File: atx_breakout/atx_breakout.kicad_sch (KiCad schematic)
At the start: 1 part, among them J1 ATX-24

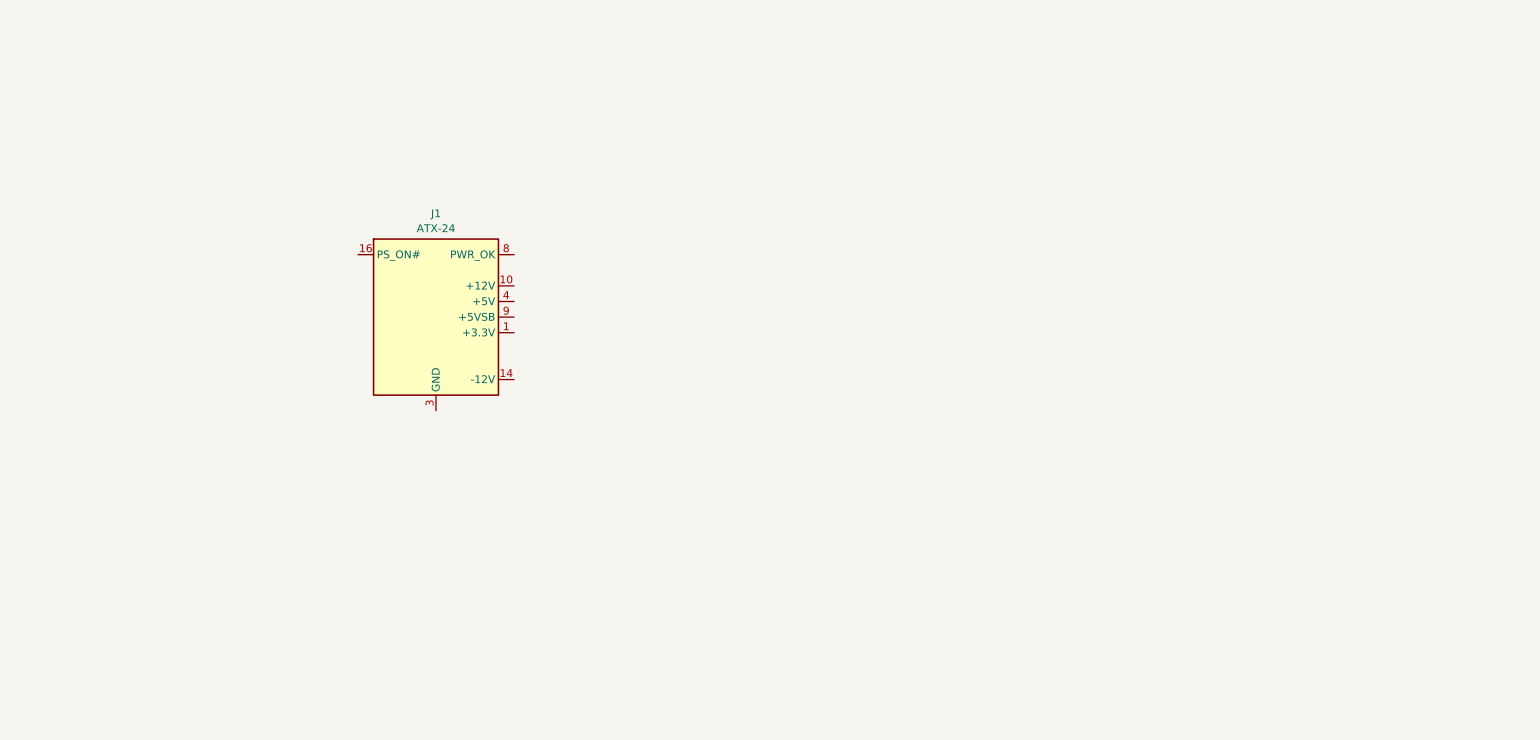
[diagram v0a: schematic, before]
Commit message: Progress on atx breakout
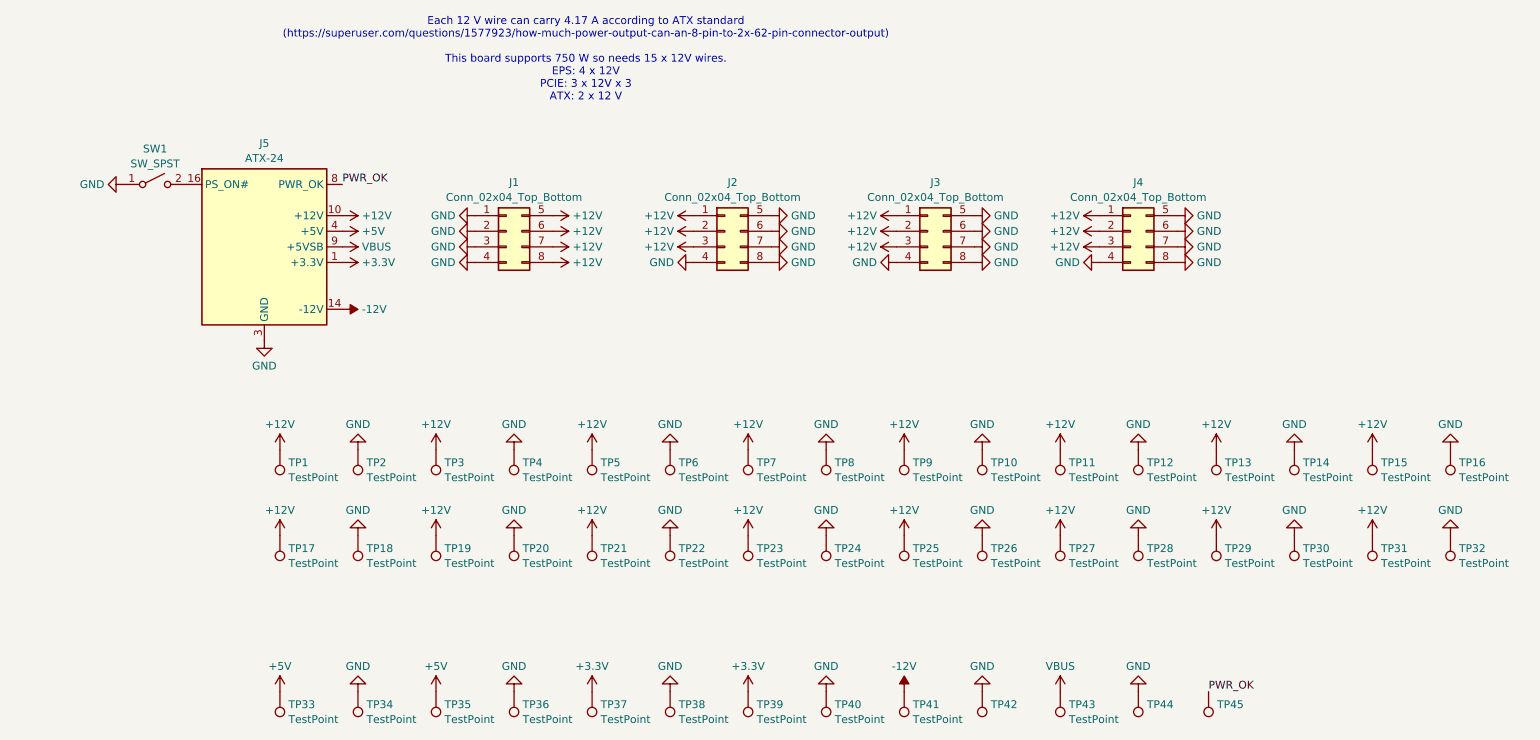
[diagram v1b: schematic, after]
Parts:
- added J1, J2, J3, J4: Conn_02x04_Top_Bottom, Connector_Molex:Molex_Mini-Fit_Jr_5566-08A_2x04_P4.20mm_Vertical, symbol Connector_Generic:Conn_02x04_Top_Bottom
- added SW1: SW_SPST, Button_Switch_THT:SW_PUSH_6mm, symbol Switch:SW_SPST
- added TP1, TP10, TP11, TP12, TP13, TP14, TP15, TP16, TP2, TP3, TP33, TP34, TP35, TP36, TP37, TP38, TP39, TP4, TP40, TP41, TP42, TP43, TP44, TP45, TP5, TP6, TP7, TP8, TP9: TestPoint, TestPoint:TestPoint_THTPad_D1.5mm_Drill0.7mm, symbol Connector:TestPoint
- added TP17, TP18, TP19, TP20, TP21, TP22, TP23, TP24, TP25, TP26, TP27, TP28, TP29, TP30, TP31, TP32: TestPoint, TestPoint:TestPoint_THTPad_D3.0mm_Drill1.5mm, symbol Connector:TestPoint
- renumbered J1 to J5
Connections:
- net +3.3V: now reaches J5.1 (+3.3V), J5.12 (+3.3V), J5.13 (+3.3V), J5.2 (+3.3V)
- net +3.3V: now also TP37.1, TP39.1
- net +12V: now reaches J5.10 (+12V), J5.11 (+12V)
- net +12V: now also J1.5 (Pin_5), J1.6 (Pin_6), J1.7 (Pin_7), J1.8 (Pin_8), J2.1 (Pin_1), J2.2 (Pin_2), J2.3 (Pin_3), J3.1 (Pin_1), J3.2 (Pin_2), J3.3 (Pin_3), J4.1 (Pin_1), J4.2 (Pin_2), J4.3 (Pin_3), TP1.1, TP11.1, TP13.1, TP15.1, TP17.1, TP19.1, TP21.1, TP23.1, TP25.1, TP27.1, TP29.1, TP3.1, TP31.1, TP5.1, TP7.1, TP9.1
- net -12V: now reaches J5.14 (-12V)
- net -12V: now also TP41.1
- net GND: now reaches J5.15 (GND), J5.17 (GND), J5.18 (GND), J5.19 (GND), J5.24 (GND), J5.3 (GND), J5.5 (GND), J5.7 (GND)
- net GND: now also J1.1 (Pin_1), J1.2 (Pin_2), J1.3 (Pin_3), J1.4 (Pin_4), J2.4 (Pin_4), J2.5 (Pin_5), J2.6 (Pin_6), J2.7 (Pin_7), J2.8 (Pin_8), J3.4 (Pin_4), J3.5 (Pin_5), J3.6 (Pin_6), J3.7 (Pin_7), J3.8 (Pin_8), J4.4 (Pin_4), J4.5 (Pin_5), J4.6 (Pin_6), J4.7 (Pin_7), J4.8 (Pin_8), SW1.1 (A), TP10.1, TP12.1, TP14.1, TP16.1, TP18.1, TP2.1, TP20.1, TP22.1, TP24.1, TP26.1, TP28.1, TP30.1, TP32.1, TP34.1, TP36.1, TP38.1, TP4.1, TP40.1, TP42.1, TP44.1, TP6.1, TP8.1
- net at J5.16 (PS_ON#): now also SW1.2 (B)
- net +5V: now reaches J5.21 (+5V), J5.22 (+5V), J5.23 (+5V), J5.4 (+5V), J5.6 (+5V)
- net +5V: now also TP33.1, TP35.1
- net PWR_OK: now reaches J5.8 (PWR_OK)
- net PWR_OK: now also TP45.1
- net VBUS: now reaches J5.9 (+5VSB)
- net VBUS: now also TP43.1
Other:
- note added: "Each 12 V wire can carry 4.17 A according to ATX standard (https://superuser.com/questions/1577923/how-much-power-output-can-an-8-pin-to-2x-62-pin-connector-output) This board supports 750 W so needs 15 x 12V wires. EPS: 4 x 12V PCIE: 3 x 12V x 3 ATX: 2 x 12 V"
- moved on the sheet: J5

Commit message: Progress on atx breakout
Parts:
- added H1: MountingHole, MountingHole:MountingHole_2.2mm_M2, symbol Mechanical:MountingHole
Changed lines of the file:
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@@
+	)
+	(symbol
+		(lib_id "Mechanical:MountingHole")
+		(at 190.5 49.53 0)
+		(unit 1)
+		(exclude_from_sim yes)
+		(in_bom no)
+		(on_board yes)
+		(dnp no)
+		(fields_autoplaced yes)
+		(property "Reference" "H1"
+			(at 193.04 48.3178 0)
+			(effects
+				(font
+					(size 1.27 1.27)
+				)
+				(justify left)
+			)
+		)
+		(property "Value" "MountingHole"
+			(at 193.04 50.7421 0)
+			(effects
+				(font
+					(size 1.27 1.27)
+				)
+				(justify left)
+			)
+		)
+		(property "Footprint" "MountingHole:MountingHole_2.2mm_M2"
+			(at 190.5 49.53 0)
+			(effects
+				(font
+					(size 1.27 1.27)
+				)
+				(hide yes)
+			)
+		)
+		(property "Datasheet" "~"
+			(at 190.5 49.53 0)
+			(effects
+				(font
+					(size 1.27 1.27)
+				)
+				(hide yes)
+			)
+		)
+		(property "Description" "Mounting Hole without connection"
+			(at 190.5 49.53 0)
+			(effects
+				(font
+					(size 1.27 1.27)
+				)
+				(hide yes)
+			)
+		)
+		(instances
+			(project ""
+				(path "/8bcbfe75-aa60-4e26-b080-e95e33d1efa7"
+					(reference "H1")
+					(unit 1)
+				)
+			)
+		)
 	)
 	(symbol

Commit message: Finished atx breakout
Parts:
- removed SW1: SW_SPST, Button_Switch_THT:SW_PUSH_6mm, symbol Switch:SW_SPST
- added U1: SW_DPDT_PS-70N, misc:SW_DPDT_PS-70N, symbol misc:SW_DPDT_PS-70N
- J1, J2, J3, J4: footprint Connector_Molex:Molex_Mini-Fit_Jr_5566-08A_2x04_P4.20mm_Vertical -> misc:Molex_Mini-Fit_Jr_5566-08A_2x04_P4.20mm_XY_Vertical
- J5: footprint Connector_Molex:Molex_Mini-Fit_Jr_5566-24A_2x12_P4.20mm_Vertical -> misc:Molex_Mini-Fit_Jr_5566-24A_2x12_P4.20mm_XY_Vertical
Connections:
- net GND: now also U1.1, U1.2, U1.4, U1.5, U1.6
- net at J5.16 (PS_ON#): now also U1.3

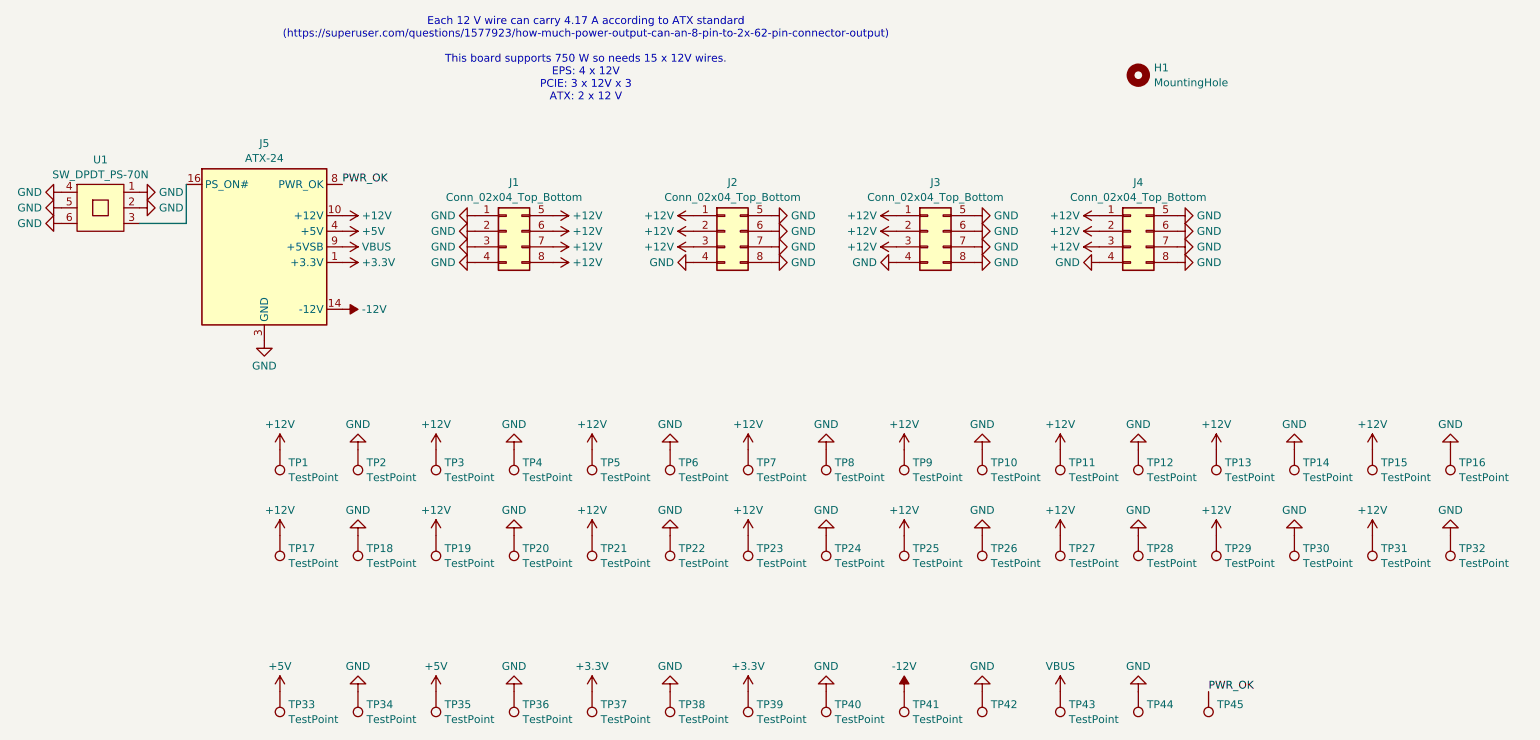
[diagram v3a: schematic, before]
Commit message: Add atx gerbers
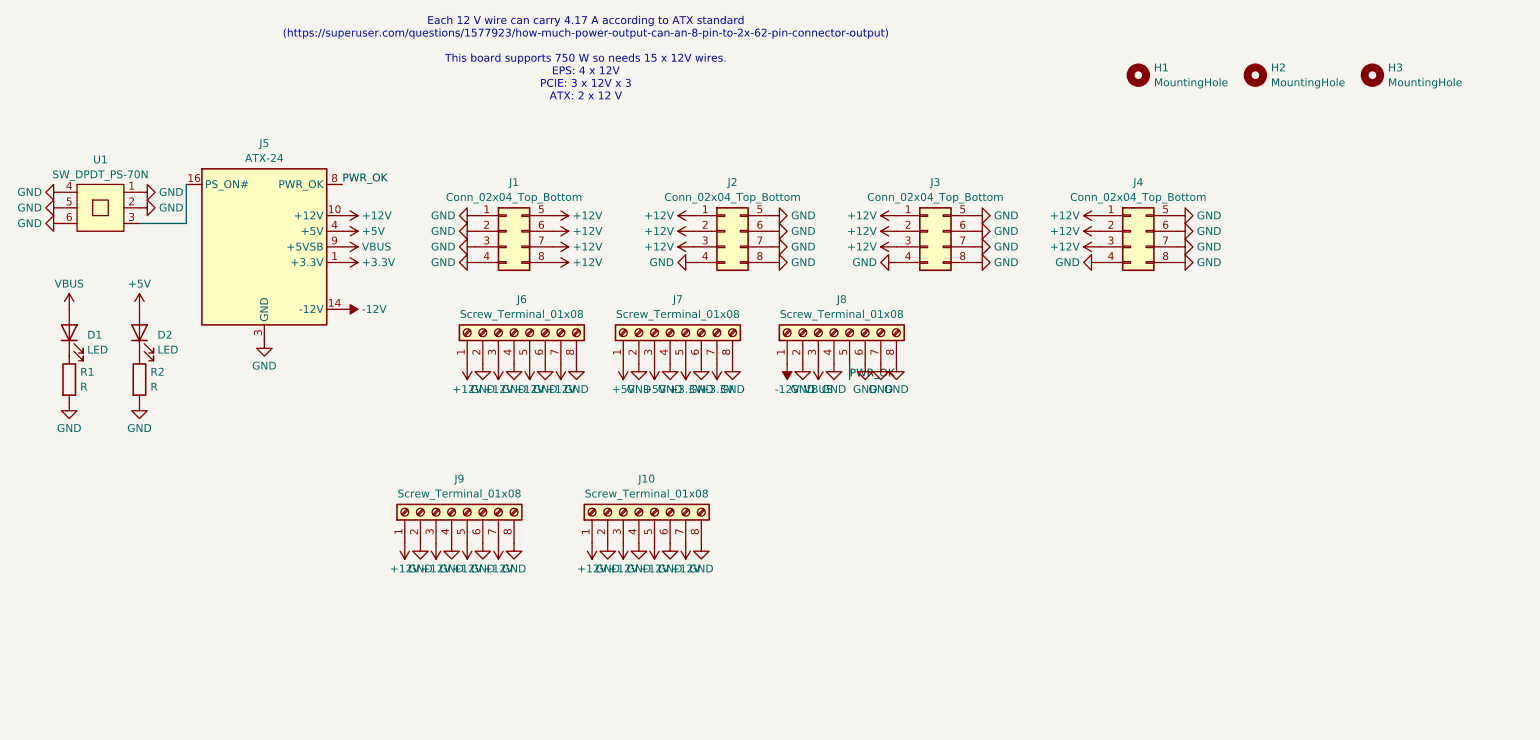
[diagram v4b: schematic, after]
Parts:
- removed TP1, TP10, TP11, TP12, TP13, TP14, TP15, TP16, TP2, TP3, TP33, TP34, TP35, TP36, TP37, TP38, TP39, TP4, TP40, TP41, TP42, TP43, TP44, TP45, TP5, TP6, TP7, TP8, TP9: TestPoint, TestPoint:TestPoint_THTPad_D1.5mm_Drill0.7mm, symbol Connector:TestPoint
- removed TP17, TP18, TP19, TP20, TP21, TP22, TP23, TP24, TP25, TP26, TP27, TP28, TP29, TP30, TP31, TP32: TestPoint, TestPoint:TestPoint_THTPad_D3.0mm_Drill1.5mm, symbol Connector:TestPoint
- added D1, D2: LED, LED_THT:LED_D5.0mm, symbol Device:LED
- added H2, H3: MountingHole, MountingHole:MountingHole_2.2mm_M2, symbol Mechanical:MountingHole
- added J10, J9: Screw_Terminal_01x08, TerminalBlock_Phoenix:TerminalBlock_Phoenix_PT-1,5-8-5.0-H_1x08_P5.00mm_Horizontal, symbol Connector:Screw_Terminal_01x08
- added J6, J7, J8: Screw_Terminal_01x08, TerminalBlock_Phoenix:TerminalBlock_Phoenix_PT-1,5-8-3.5-H_1x08_P3.50mm_Horizontal, symbol Connector:Screw_Terminal_01x08
- added R1, R2: R, Resistor_THT:R_Axial_DIN0207_L6.3mm_D2.5mm_P7.62mm_Horizontal, symbol Device:R
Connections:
- net +12V: now also J10.1 (Pin_1), J10.3 (Pin_3), J10.5 (Pin_5), J10.7 (Pin_7), J6.1 (Pin_1), J6.3 (Pin_3), J6.5 (Pin_5), J6.7 (Pin_7), J9.1 (Pin_1), J9.3 (Pin_3), J9.5 (Pin_5), J9.7 (Pin_7)
- net +3.3V: now also J7.5 (Pin_5), J7.7 (Pin_7)
- net +5V: now also D2.2 (A), J7.1 (Pin_1), J7.3 (Pin_3)
- net -12V: now also J8.1 (Pin_1)
- net GND: now also J10.2 (Pin_2), J10.4 (Pin_4), J10.6 (Pin_6), J10.8 (Pin_8), J6.2 (Pin_2), J6.4 (Pin_4), J6.6 (Pin_6), J6.8 (Pin_8), J7.2 (Pin_2), J7.4 (Pin_4), J7.6 (Pin_6), J7.8 (Pin_8), J8.2 (Pin_2), J8.4 (Pin_4), J8.6 (Pin_6), J8.7 (Pin_7), J8.8 (Pin_8), J9.2 (Pin_2), J9.4 (Pin_4), J9.6 (Pin_6), J9.8 (Pin_8), R1.2, R2.2
- net PWR_OK: now also J8.5 (Pin_5)
- net VBUS: now also D1.2 (A), J8.3 (Pin_3)
- new net: D1.1 (K), R1.1
- new net: D2.1 (K), R2.1
